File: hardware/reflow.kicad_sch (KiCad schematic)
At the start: 45 parts, among them K1 OZ-SS-112L1, K2 OZ-SS-112L1, K3 SDT-SS-112DM, K4 0J-SS-112LWHF, Q1 RE1C002UNTCL, Q2 RE1C002UNTCL, Q3 RE1C002UNTCL, Q4 RE1C002UNTCL, U1 ESP-12E, U2 AD8495

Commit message: updated kicad files
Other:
- moved on the sheet: C1, C2, R10, R11, R12, R5, R6, R8, R9, U1

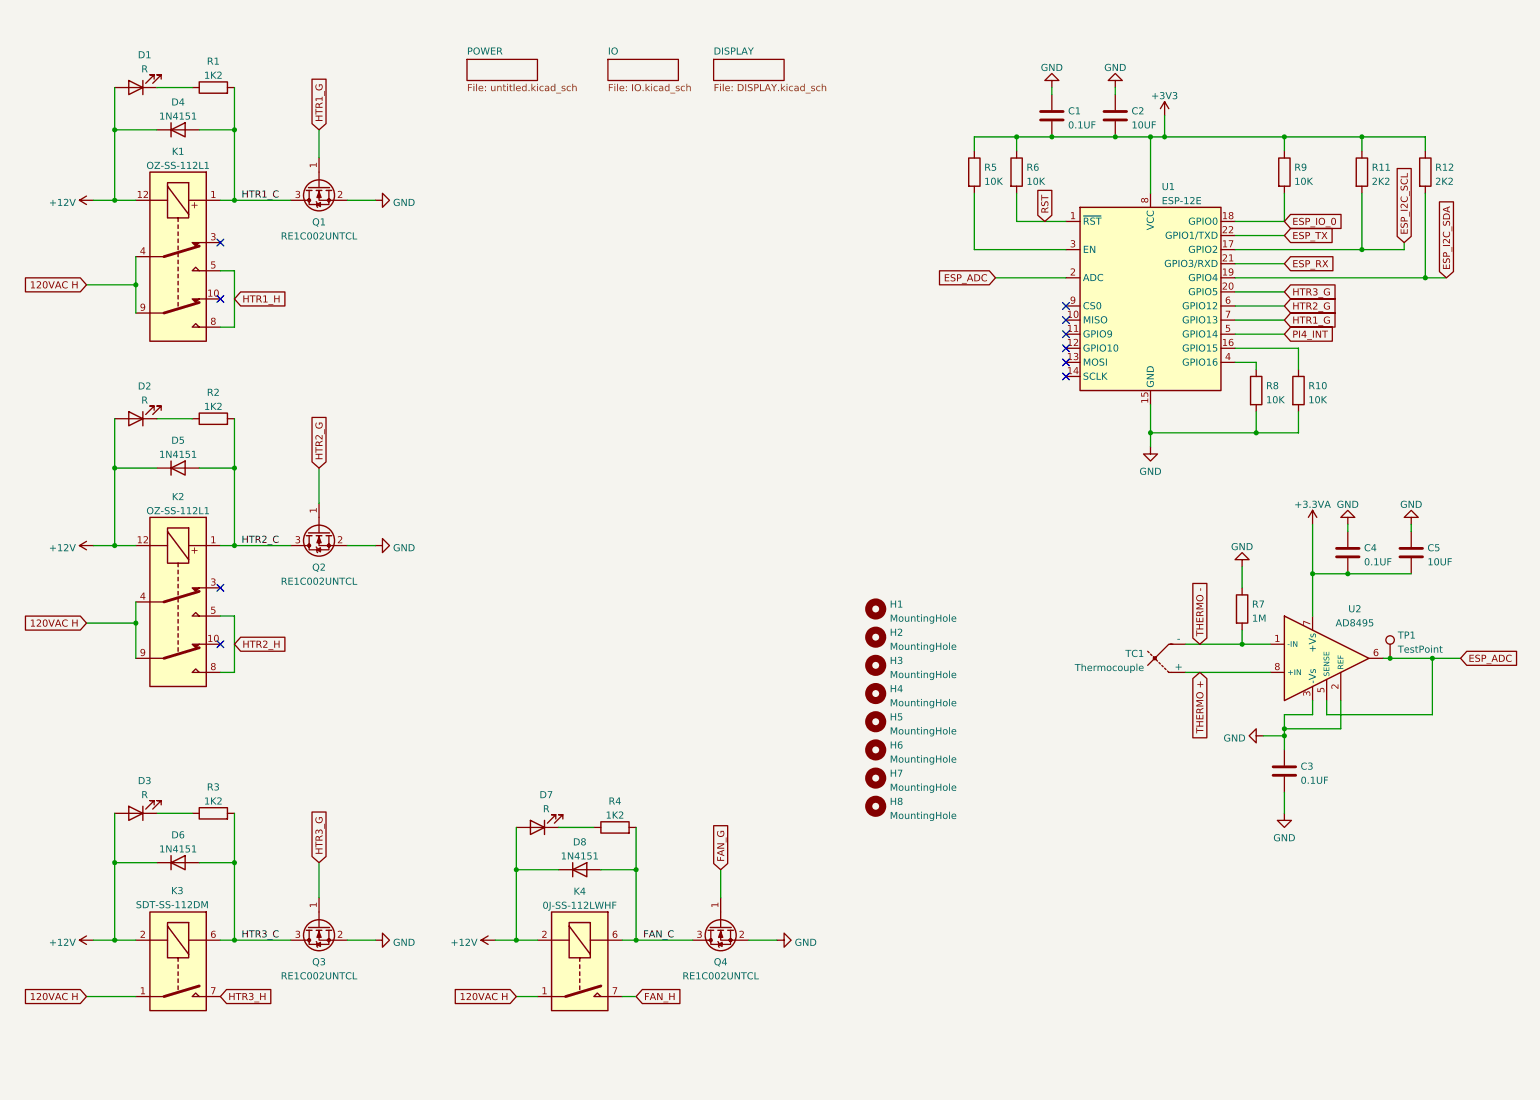
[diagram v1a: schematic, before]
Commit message: updated hardware schimatics for better readability
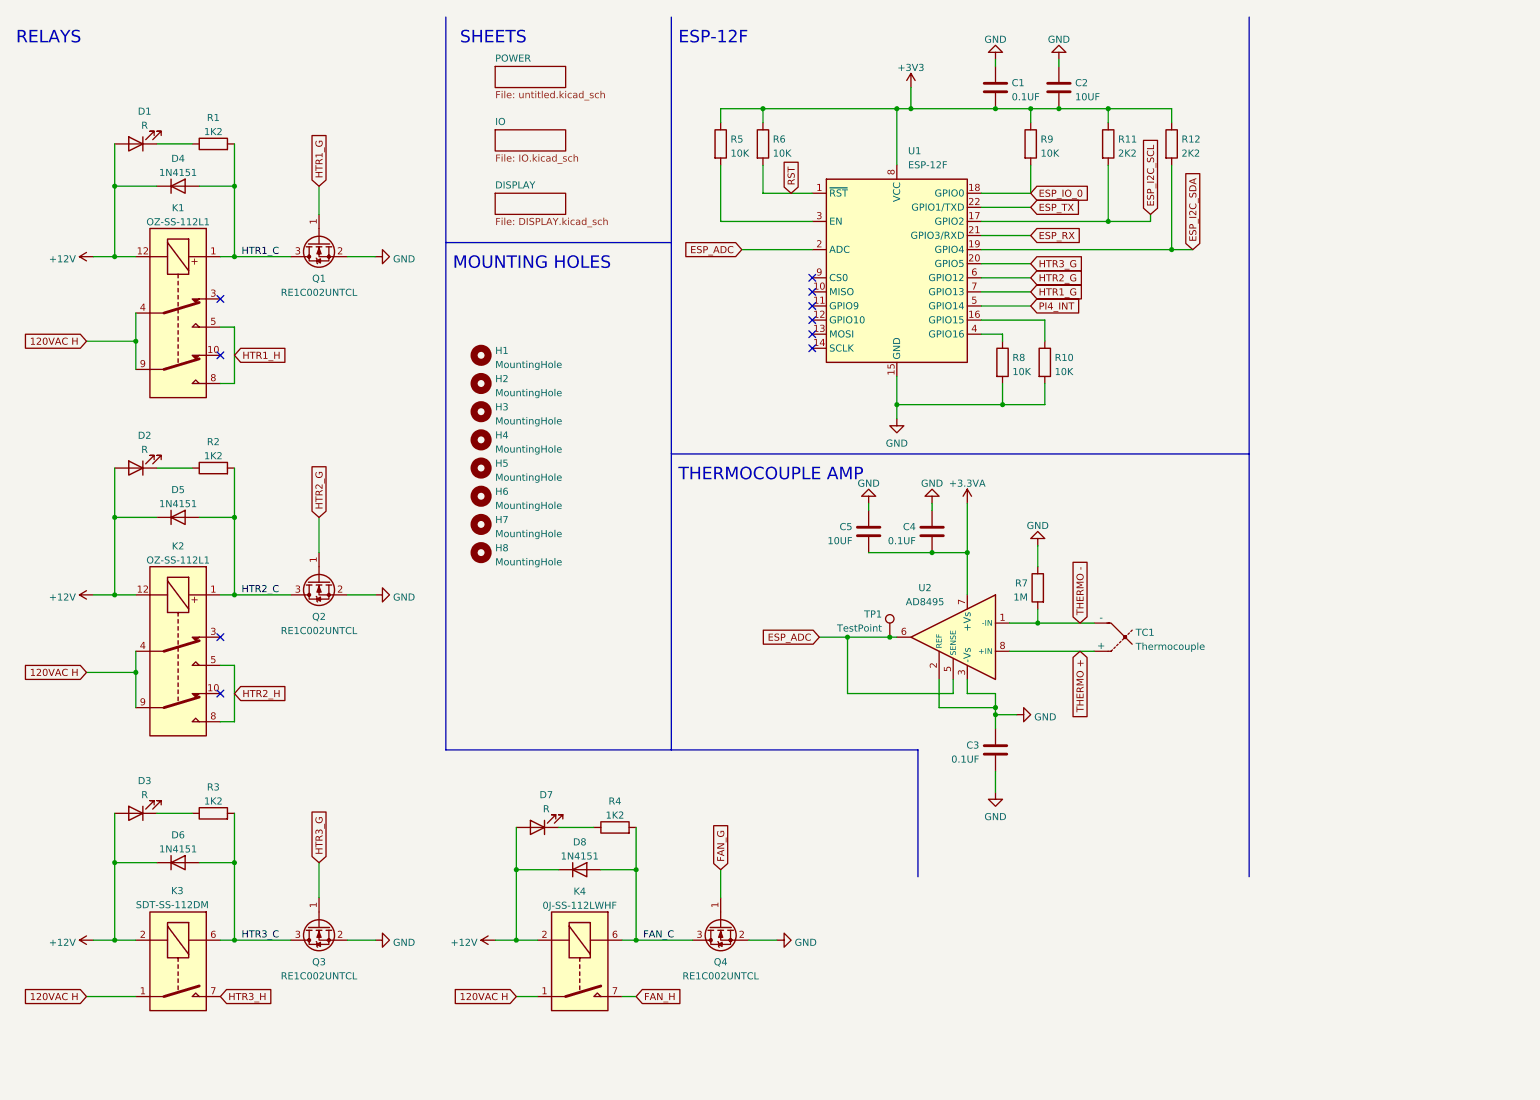
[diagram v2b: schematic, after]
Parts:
- U1: value ESP-12E -> ESP-12F
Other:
- note added: "ESP-12F"
- note added: "MOUNTING HOLES"
- note added: "RELAYS"
- note added: "SHEETS"
- note added: "THERMOCOUPLE AMP"
- moved on the sheet: C1, C2, C3, C4, C5, D1, D2, D4, D5, H1, H2, H3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

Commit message: added a voltage devider for the dcinput on the esp
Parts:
- added R24: 660R, symbol Device:R
- added R25: 330R, symbol Device:R
- added TP16, TP17, TP18, TP19, TP20, TP21: TestPoint, symbol Connector:TestPoint
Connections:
- net HTR3_G is gone; now on net FAN_G: Q3.1 (G), U1.20 (GPIO5)
- net HTR3_H is gone; now on net FAN_H: K3.7, K3.8
- net ESP_ADC: now also R24.2, R25.1, TP20.1; no longer TP1.1, U2.5 (SENSE), U2.6
- net FAN_C: now also D6.2 (A), K3.6, Q3.3 (S), R3.2, TP18.1; no longer D8.2 (A), K4.6, Q4.3 (S), R4.2
- net FAN_G: no longer Q4.1 (G)
- net FAN_H: no longer K4.7, K4.8
- net GND: now also R25.2
- net HTR1_C: now also TP16.1
- net HTR2_C: now also TP17.1
- removed net HTR3_C: D6.2 (A), K3.6, Q3.3 (S), R3.2
- new net LIGHT_C: D8.2 (A), K4.6, Q4.3 (S), R4.2, TP19.1
- new net LIGHT_G: Q4.1 (G)
- new net LIGHT_H: K4.7, K4.8
- new net THERMO_AMP: R24.1, TP1.1, U2.5 (SENSE), U2.6
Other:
- moved on the sheet: C1, C2, R10, R11, R12, R5, R6, R8, R9, U1

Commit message: more hardware revisions
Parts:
- removed TP21: TestPoint, symbol Connector:TestPoint
- R24, R25: footprint (none) -> Resistor_SMD:R_0603_1608Metric
- TP16, TP17, TP18, TP19, TP20: footprint (none) -> TestPoint:TestPoint_Pad_D2.0mm
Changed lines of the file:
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@@
       (effects (font (size 1.27 1.27)) (justify left))
     )
-    (property "Footprint" "" (id 2) (at 53.34 171.45 0)
+    (property "Footprint" "TestPoint:TestPoint_Pad_D2.0mm" (id 2) (at 53.34 171.45 0)
       (effects (font (size 1.27 1.27)) hide)
     )
@@
       (effects (font (size 1.27 1.27)) (justify left))
     )
-    (property "Footprint" "" (id 2) (at 135.382 44.45 90)
+    (property "Footprint" "Resistor_SMD:R_0603_1608Metric" (id 2) (at 135.382 44.45 90)
       (effects (font (size 1.27 1.27)) hide)
     )
@@
     (pin "1")
   )
-  (symbol (lib_id "Connector:TestPoint") (at 167.64 201.93 270) (unit 1)
-    (in_bom yes) (on_board yes) (fields_autoplaced)
-    (property "Reference" "TP21" (id 0) (at 172.72 200.6599 90)
-      (effects (font (size 1.27 1.27)) (justify left))
-    )
-    (property "Value" "TestPoint" (id 1) (at 172.72 203.1999 90)
-      (effects (font (size 1.27 1.27)) (justify left))
-    )
-    (property "Footprint" "" (id 2) (at 167.64 207.01 0)
-      (effects (font (size 1.27 1.27)) hide)
-    )
-    (property "Datasheet" "~" (id 3) (at 167.64 207.01 0)
-      (effects (font (size 1.27 1.27)) hide)
-    )
-    (pin "1")
-  )
   (symbol (lib_id "power:GND") (at 78.74 54.61 90) (unit 1)
     (in_bom yes) (on_board yes) (fields_autoplaced)
@@
       (effects (font (size 1.27 1.27)) (justify left))
     )
-    (property "Footprint" "" (id 2) (at 125.73 172.72 0)
+    (property "Footprint" "TestPoint:TestPoint_Pad_D2.0mm" (id 2) (at 125.73 172.72 0)
       (effects (font (size 1.27 1.27)) hide)
     )
@@
       (effects (font (size 1.27 1.27)) (justify left))
     )
-    (property "Footprint" "" (id 2) (at 135.382 59.69 90)
+    (property "Footprint" "Resistor_SMD:R_0603_1608Metric" (id 2) (at 135.382 59.69 90)
       (effects (font (size 1.27 1.27)) hide)
     )
@@
       (effects (font (size 1.27 1.27)) (justify left))
     )
-    (property "Footprint" "" (id 2) (at 53.34 110.49 0)
+    (property "Footprint" "TestPoint:TestPoint_Pad_D2.0mm" (id 2) (at 53.34 110.49 0)
       (effects (font (size 1.27 1.27)) hide)
     )
@@
       (effects (font (size 1.27 1.27)) (justify right))
     )
-    (property "Footprint" "" (id 2) (at 146.05 52.07 0)
+    (property "Footprint" "TestPoint:TestPoint_Pad_D2.0mm" (id 2) (at 146.05 52.07 0)
       (effects (font (size 1.27 1.27)) hide)
     )
@@
       (effects (font (size 1.27 1.27)) (justify left))
     )
-    (property "Footprint" "" (id 2) (at 53.34 48.26 0)
+    (property "Footprint" "TestPoint:TestPoint_Pad_D2.0mm" (id 2) (at 53.34 48.26 0)
       (effects (font (size 1.27 1.27)) hide)
     )
@@
     )
     (path "/9e9c5bab-137b-4e96-8dfe-18bd3679817b/21fdee44-366b-45a5-bc0e-891753e0d731"
-      (reference "J2") (unit 1) (value "Screw_Terminal_01x06") (footprint "")
+      (reference "J2") (unit 1) (value "Screw_Terminal_01x06") (footprint "EXTRA:SCREW_TERM_5MM_7")
     )
     (path "/9e9c5bab-137b-4e96-8dfe-18bd3679817b/c95ef3aa-6645-42cb-abf4-f215338b0881"
@@
     )
     (path "/3d256a48-2f00-4c2c-a734-1d473649c30d"
-      (reference "R24") (unit 1) (value "660R") (footprint "")
+      (reference "R24") (unit 1) (value "660R") (footprint "Resistor_SMD:R_0603_1608Metric")
     )
     (path "/9038edf0-db9c-4acb-bfb3-57c9af7f3c02"
-      (reference "R25") (unit 1) (value "330R") (footprint "")
+      (reference "R25") (unit 1) (value "330R") (footprint "Resistor_SMD:R_0603_1608Metric")
     )
     (path "/9e9c5bab-137b-4e96-8dfe-18bd3679817b/f3906cfe-d892-4654-9be4-861ac908d343"
@@
     )
     (path "/e9989f32-1ffb-4b19-96eb-be2a5373d230"
-      (reference "TP16") (unit 1) (value "TestPoint") (footprint "")
+      (reference "TP16") (unit 1) (value "TestPoint") (footprint "TestPoint:TestPoint_Pad_D2.0mm")
     )
     (path "/9f5ebb80-291c-4281-bf1e-4c74782b9831"
-      (reference "TP17") (unit 1) (value "TestPoint") (footprint "")
+      (reference "TP17") (unit 1) (value "TestPoint") (footprint "TestPoint:TestPoint_Pad_D2.0mm")
     )
     (path "/07eb78bb-8505-4e19-88fa-0f5a42086570"
-      (reference "TP18") (unit 1) (value "TestPoint") (footprint "")
+      (reference "TP18") (unit 1) (value "TestPoint") (footprint "TestPoint:TestPoint_Pad_D2.0mm")
     )
     (path "/78d4ae6a-4bfc-42bd-977e-eaee62c2fb33"
-      (reference "TP19") (unit 1) (value "TestPoint") (footprint "")
+      (reference "TP19") (unit 1) (value "TestPoint") (footprint "TestPoint:TestPoint_Pad_D2.0mm")
     )
     (path "/d3090971-cbeb-4b24-8c53-4014215f0f8b"
-      (reference "TP20") (unit 1) (value "TestPoint") (footprint "")
-    )
-    (path "/528901f9-ad79-43b2-a8d9-80743ccf2fee"
-      (reference "TP21") (unit 1) (value "TestPoint") (footprint "")
+      (reference "TP20") (unit 1) (value "TestPoint") (footprint "TestPoint:TestPoint_Pad_D2.0mm")
     )
     (path "/b522862e-bc48-47cf-bf94-97458c8d292b/dd1fbf00-1f19-418e-b385-0ce6150dd5f6"

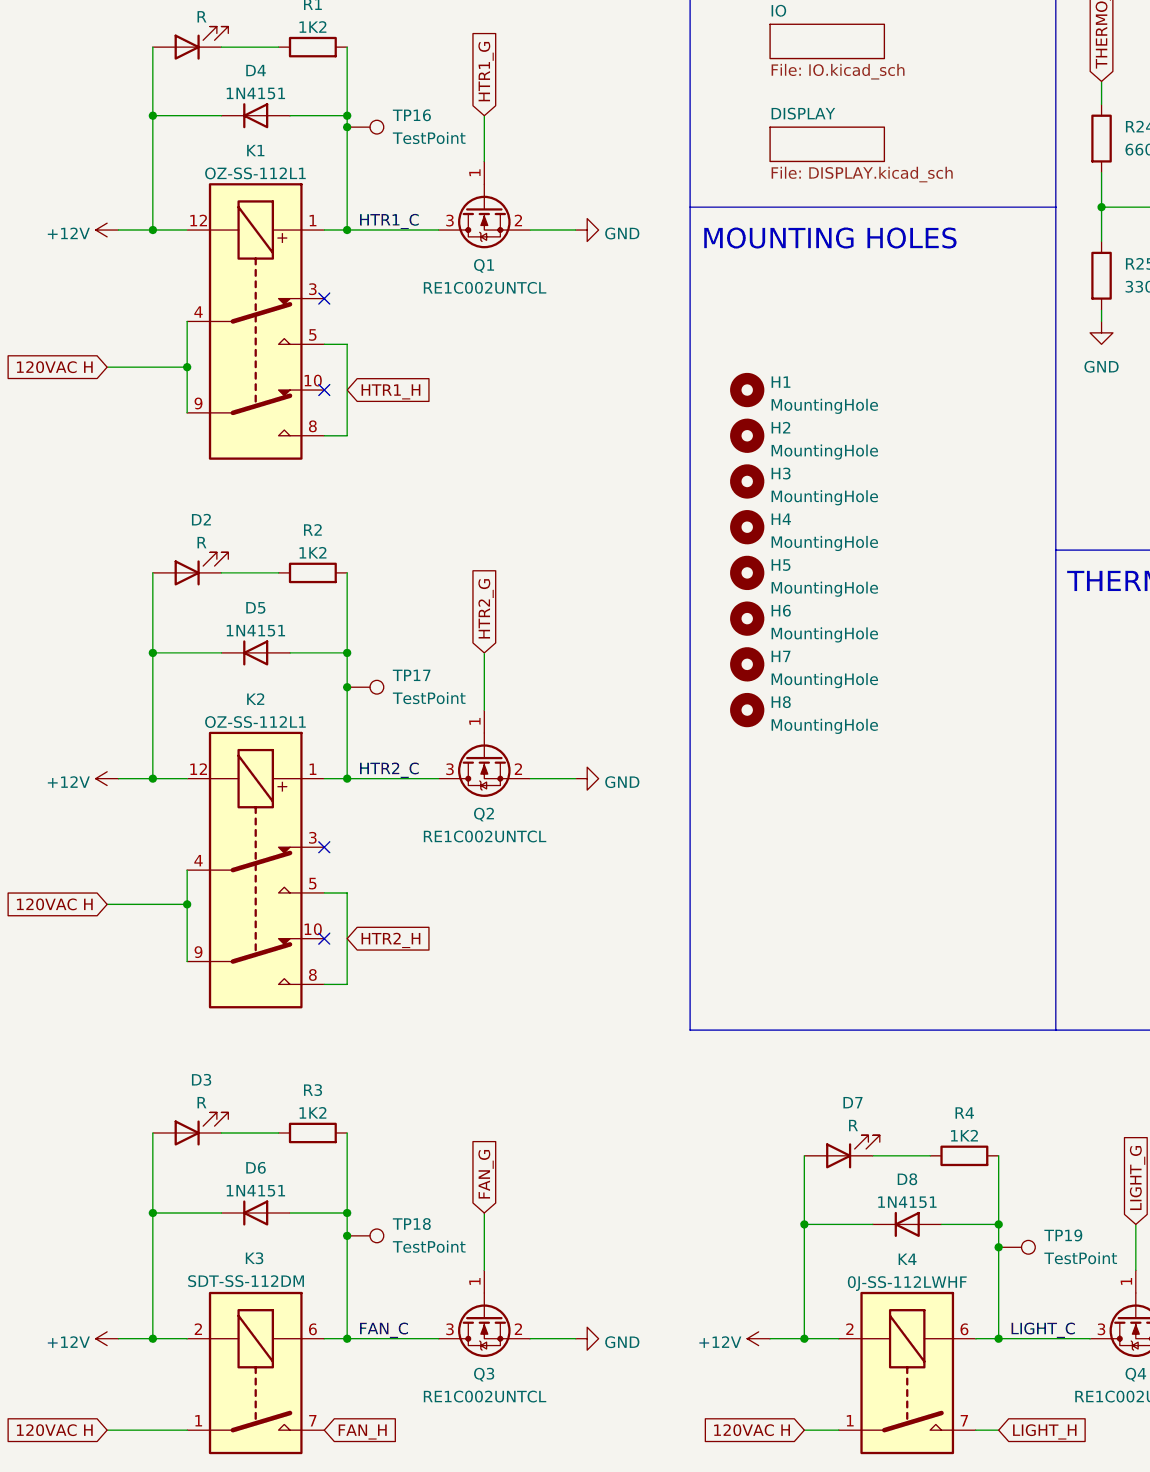
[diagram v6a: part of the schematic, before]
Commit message: major hardware refctoring to use modern parts that are still being made
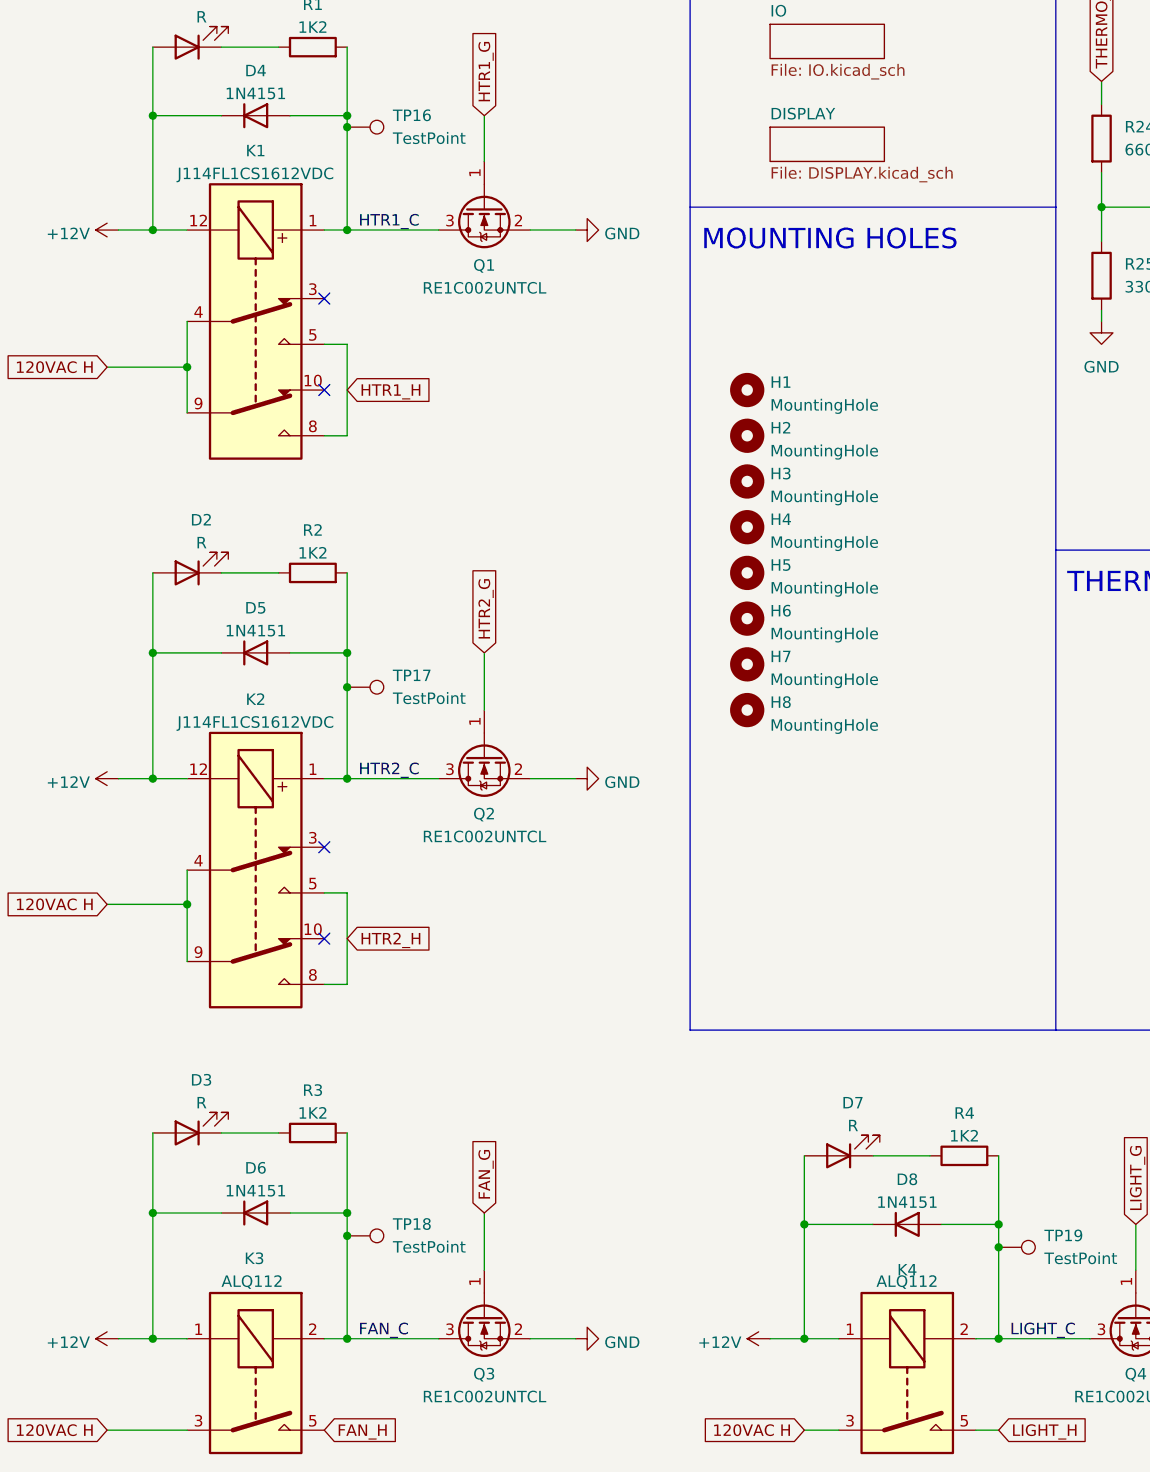
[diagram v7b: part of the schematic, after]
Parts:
- K1, K2: value OZ-SS-112L1 -> J114FL1CS1612VDC; footprint EXTRA:0Z-SS-112L1 -> EXTRA:J114FL1CS1612VDC
- K3: value SDT-SS-112DM -> ALQ112; footprint EXTRA:SDT-SS-112DM -> EXTRA:RELAY_ALQ112
- K4: value 0J-SS-112LWHF -> ALQ112; footprint EXTRA:0J-SS-112LWHF -> EXTRA:RELAY_ALQ112
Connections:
- net +12V: now also K3.1, K4.1; no longer K3.2, K4.2
- net 120VAC H: now also K3.3, K4.3; no longer K3.1, K4.1
- net FAN_C: now also K3.2; no longer K3.6
- net FAN_H: now also K3.5; no longer K3.7
- net LIGHT_C: now also K4.2; no longer K4.6
- net LIGHT_H: now also K4.5; no longer K4.7
